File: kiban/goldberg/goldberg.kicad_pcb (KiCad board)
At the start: 2 copper layers, 68.5 x 85.4 mm, 162 parts, among them J1 IN, J2 OUT

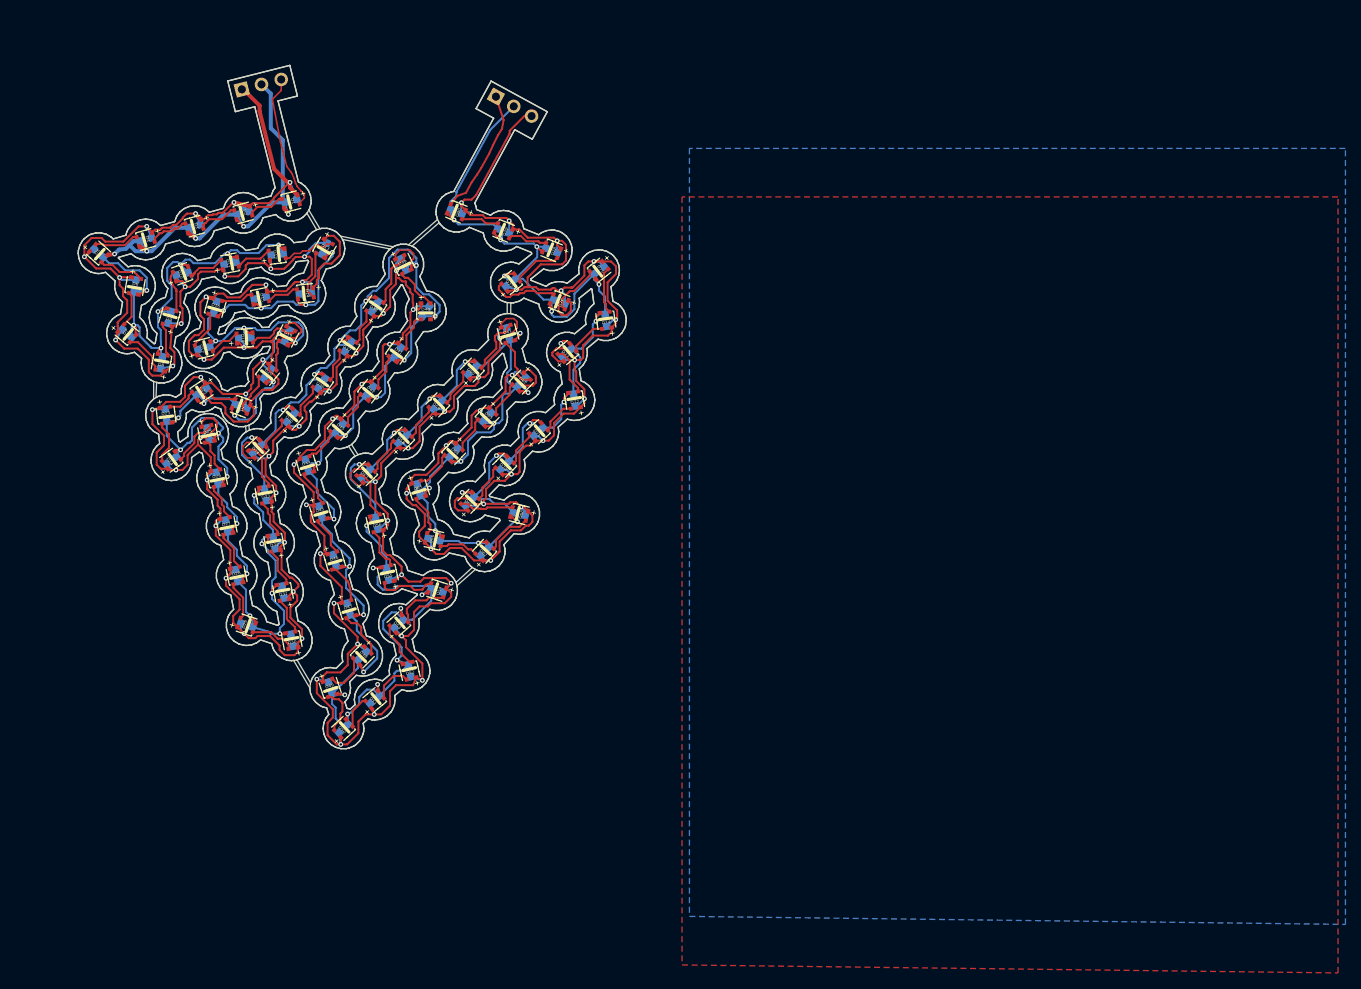
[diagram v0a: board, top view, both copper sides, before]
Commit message: feat: goldberg の LED パッドを LCSC の寸法 (0.8 x 0.8) にして配線を引き直した版
- LED (C55109522) の足型のパッドを LCSC の原本の寸法にした (ステンシルでのリフローをしやすくするため)
- 配線を引き直し、クリアランス違反・短絡・未接続を解消 (DRC: 未接続 0、照合の差は J1 / J2 の 5 件のみ)
- swap_led_v6.py: 入れ替え済みの PCB でもパッド寸法を変えられるようにした (--force)

Co-Authored-By: Claude Sonnet 5.5 <noreply@anthropic.com>
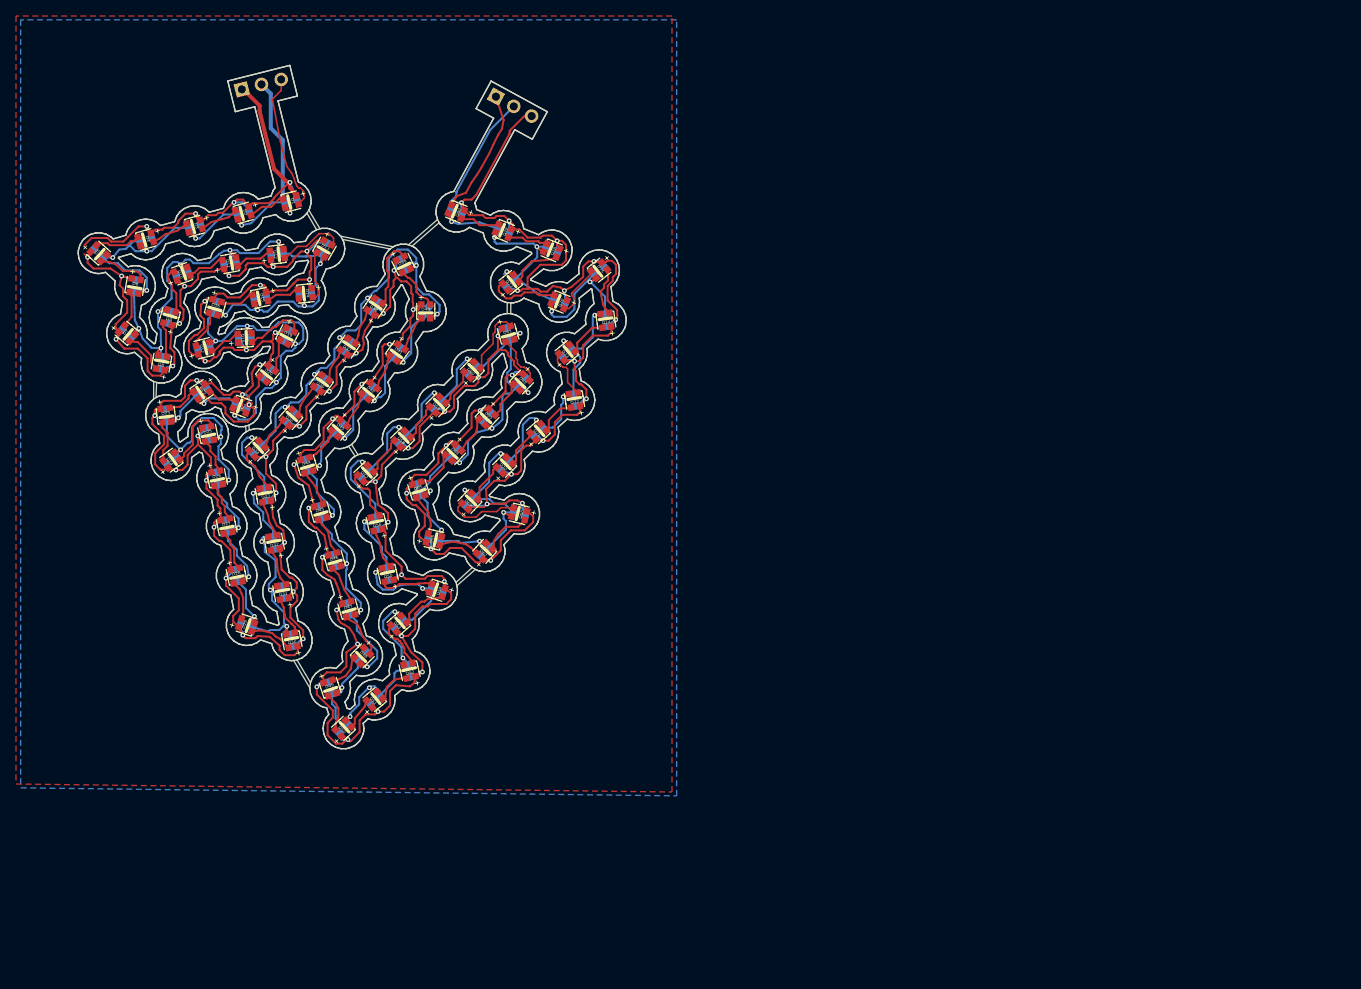
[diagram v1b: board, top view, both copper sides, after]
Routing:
- net VDD: track 855.3 -> 792.9 mm, vias 80 -> 81
- net GND: track 743.5 -> 746.0 mm
- net Net-(D68-DO): track 6.83 -> 8.95 mm
- net Net-(D12-DO): track 6.83 -> 8.55 mm
- net OUT3: track 6.30 -> 7.92 mm
- net Net-(D38-DO): track 7.22 -> 8.66 mm
- net Net-(D18-DO): track 6.49 -> 7.53 mm
- net OUT6: track 5.33 -> 4.28 mm
- net Net-(D60-DO): track 7.49 -> 8.40 mm
- net Net-(D49-DO): track 5.95 -> 5.07 mm
- net Net-(D10-DI): track 5.22 -> 5.95 mm
- net Net-(D53-DO): track 6.89 -> 6.17 mm
- net Net-(D54-DO): track 7.26 -> 6.64 mm
- net Net-(D51-DO): track 5.10 -> 4.51 mm
